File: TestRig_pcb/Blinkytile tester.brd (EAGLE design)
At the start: 160 x 140 mm, 142 parts, among them IC1 LM317BD2T, IC10 LM317BD2T, IC11 LM317BD2T, IC12 LM317BD2T, IC13 LM317BD2T, IC14 LM317BD2T, IC15 LM317BD2T, IC16 LM317BD2T, IC2 LM317BD2T, IC3 LM317BD2T, IC4 LM317BD2T, IC5 LM317BD2T, IC6 LM317BD2T, IC7 LM317BD2T, IC8 LM317BD2T, IC9 LM317BD2T, X1 MINI-USB_4P-85-32004-10X

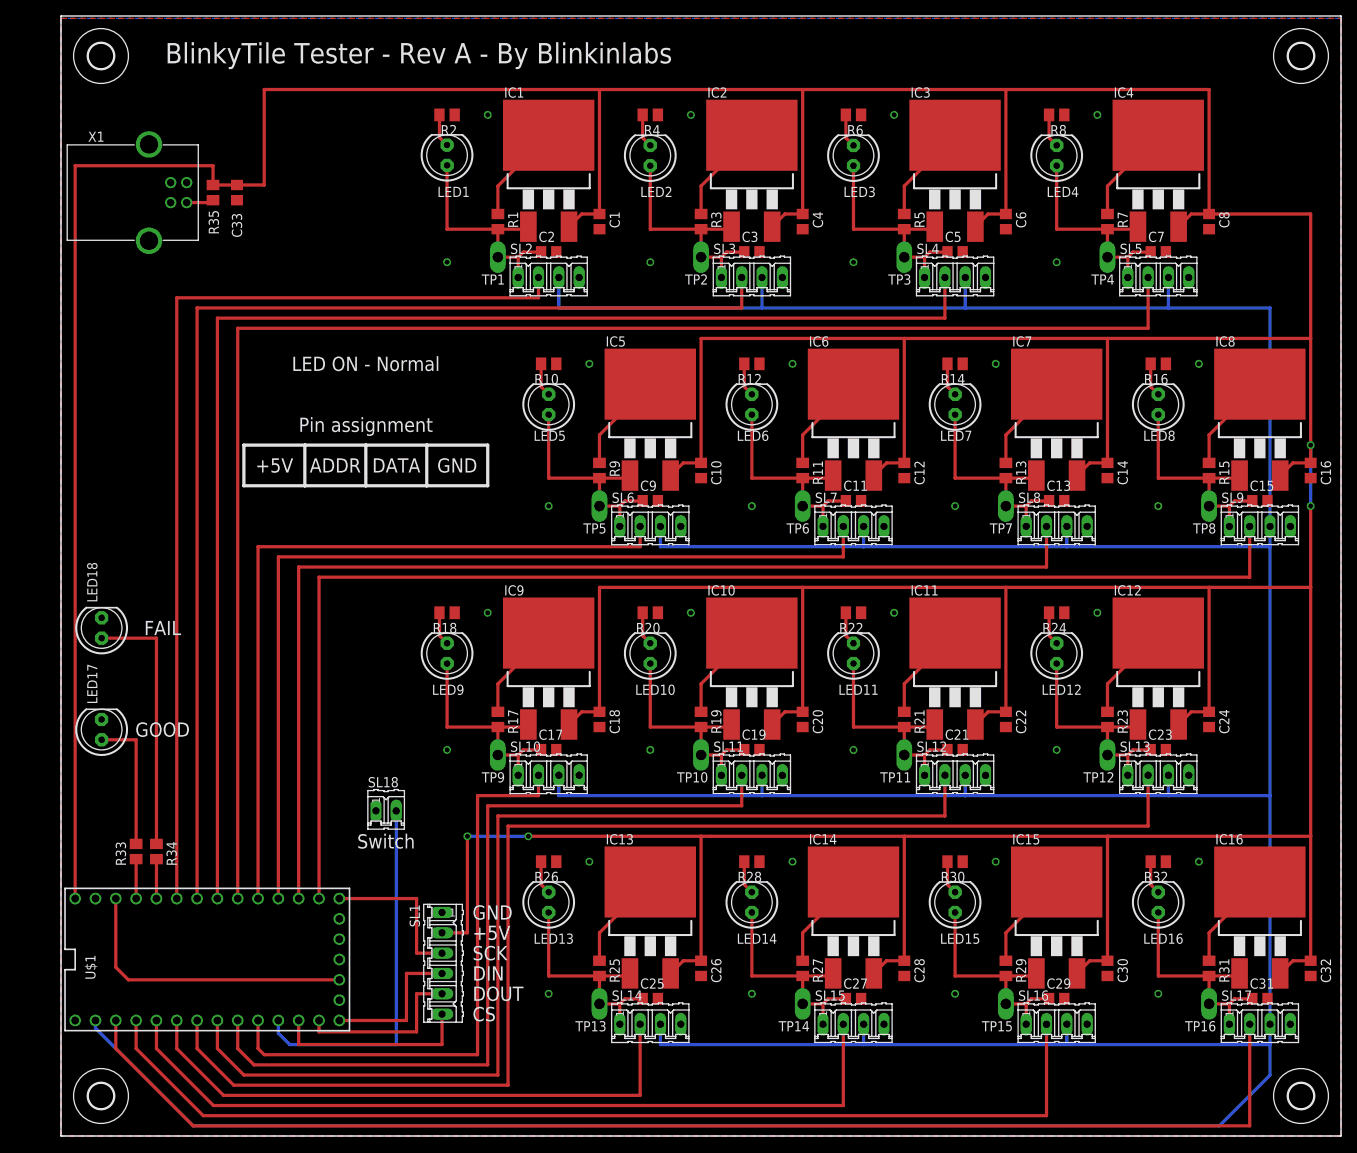
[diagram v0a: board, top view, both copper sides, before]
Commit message: RevB of tester board: add 5v buffers
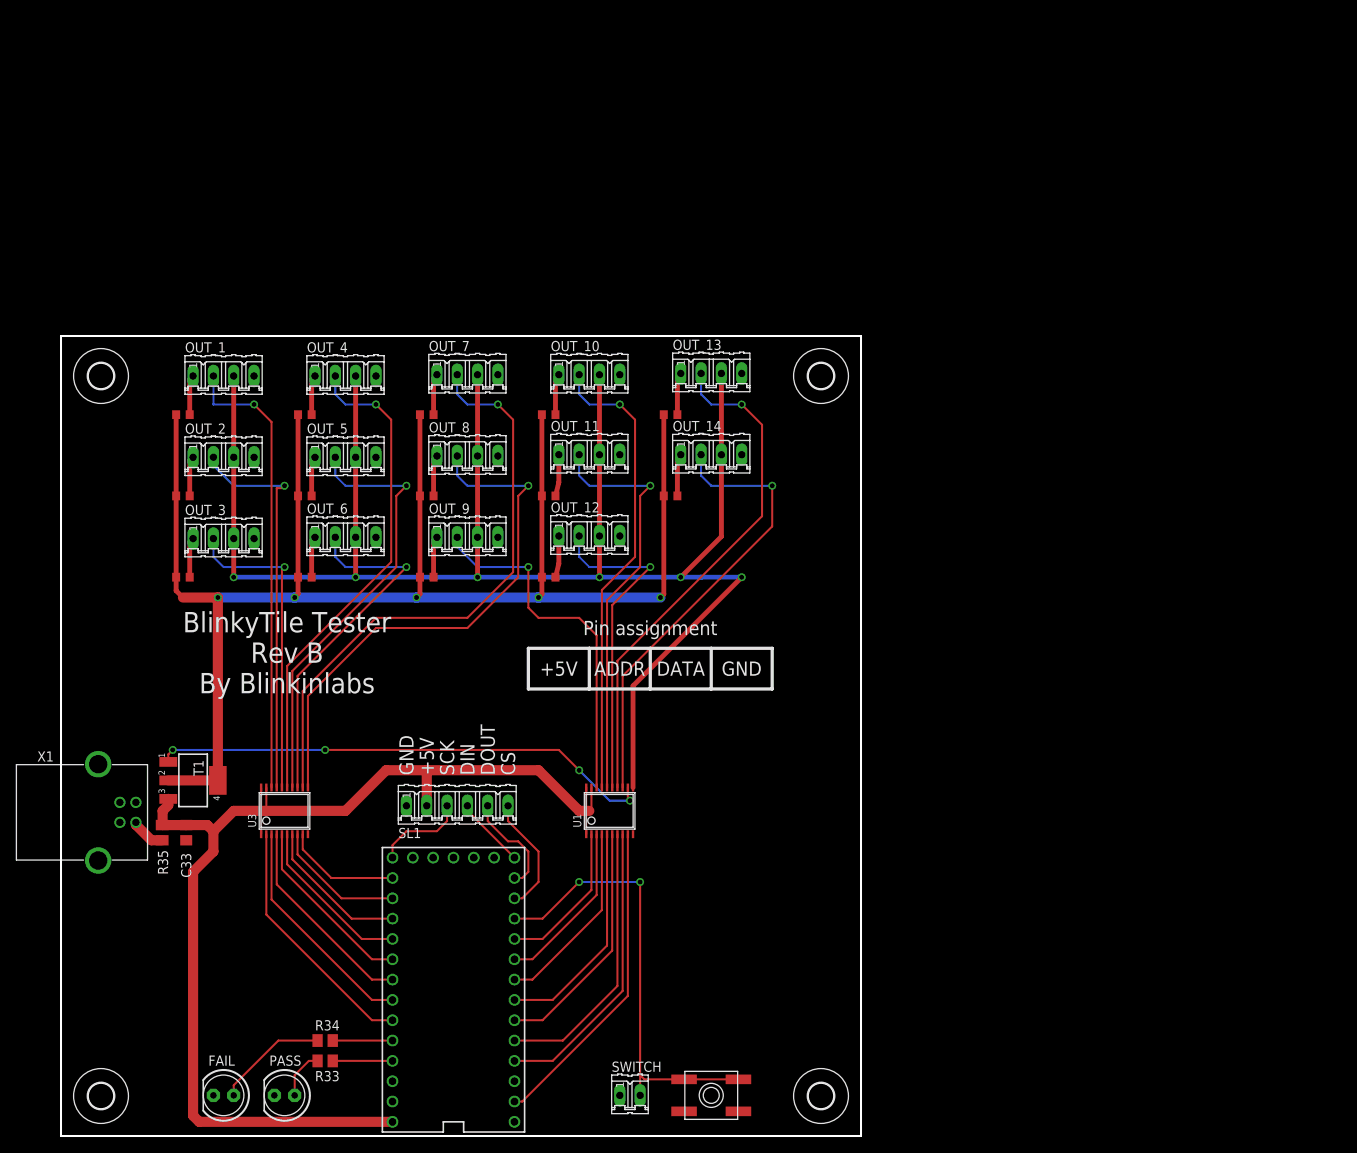
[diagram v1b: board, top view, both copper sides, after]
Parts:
- removed C1, C10, C11, C12, C13, C14, C15, C16, C17, C18, C19, C2, C20, C21, C22, C23, C24, C25, C26, C27, C28, C29, C3, C30, C31, C32, C4, C5, C6, C7, C8, C9: 0.1uF, rcl:C0805
- removed IC1, IC10, IC11, IC12, IC13, IC14, IC15, IC16, IC2, IC3, IC4, IC5, IC6, IC7, IC8, IC9: LM317BD2T, v-reg:D2PACK
- removed LED1, LED10, LED11, LED12, LED13, LED14, LED15, LED16, LED2, LED3, LED4, LED5, LED6, LED7, LED8, LED9: RED, adafruit:LED5MM
- removed LED17, LED18: (no value), adafruit:LED5MM
- removed R15, R16, R17, R18, R19, R20, R21, R22, R23, R24, R25, R26, R27, R28, R29, R30, R31, R32: (no value), rcl:M0805
- removed SL10, SL11, SL12, SL13, SL14, SL15, SL16, SL17, SL2, SL3, SL4, SL5, SL6, SL7, SL8, SL9: (no value), con-amp-quick:04P
- removed SL18: (no value), con-amp-quick:02P
- removed TP1, TP10, TP11, TP12, TP13, TP14, TP15, TP16, TP2, TP3, TP4, TP5, TP6, TP7, TP8, TP9: TPPAD1-13Y, testpad:P1-13Y
- added FAIL, PASS: (no value), adafruit:LED5MM
- added OUT_1, OUT_10, OUT_11, OUT_12, OUT_13, OUT_14, OUT_2, OUT_3, OUT_4, OUT_5, OUT_6, OUT_7, OUT_8, OUT_9: (no value), con-amp-quick:04P
- added SW1: SPST_TACT-EVQQ2, adafruit:EVQ-Q2
- added SWITCH: (no value), con-amp-quick:02P
- added T1: (no value), zetex:SOT223
- added U1, U3: SN74HCT245PWR, scanlime:TSSOP20
- R1, R10, R11, R12, R13, R14, R2, R3, R4, R5, R6, R7, R8, R9: value (none) -> 50; device rcl:M0805 -> adafruit:R0603
- moved R8 92.0 mm to (45.7, 80.0), turned to 0 degrees
- moved R6 89.7 mm to (30.5, 69.8), turned to 0 degrees
- moved R7 88.4 mm to (45.7, 90.2), turned to 0 degrees
- moved R5 82.4 mm to (30.5, 80.0), turned to 0 degrees
- moved C33 80.3 mm to (15.7, 37.9)
- moved R35 80.3 mm to (12.7, 37.9)
- moved R3 78.6 mm to (15.2, 69.8), turned to 0 degrees
- moved X1 77.7 mm to (4.65, 40.5)
- moved H3 72.1 mm to (95.0, 95.0)
- moved H4 60.0 mm to (95.0, 5.00)
- moved R2 58.0 mm to (15.2, 80.0), turned to 0 degrees
- moved R4 57.2 mm to (30.5, 90.2), turned to 0 degrees
- moved R1 46.2 mm to (15.2, 90.2), turned to 0 degrees
- moved R13 42.5 mm to (76.2, 90.2), turned to 0 degrees
- moved H2 40.0 mm to (5.00, 95.0)
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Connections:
- removed net ADDR15: SL16.2, U$1.2
- removed net ADDR16: SL17.2, U$1.1
- removed net N$10: IC4.2, R7.1
- removed net N$12: LED4.K, R8.2
- removed net N$13: IC5.2, R9.1
- removed net N$14: C9.1, IC5.1, LED5.A, R9.2, SL6.1, TP5.TP
- removed net N$15: LED5.K, R10.2
- removed net N$16: IC6.2, R11.1
- removed net N$18: LED6.K, R12.2
- removed net N$19: IC7.2, R13.1
- removed net N$21: LED7.K, R14.2
- removed net N$22: IC8.2, R15.1
- removed net N$24: LED8.K, R16.2
- removed net N$25: IC9.2, R17.1
- removed net N$27: LED9.K, R18.2
- removed net N$28: IC10.2, R19.1
- removed net N$30: LED10.K, R20.2
- removed net N$31: IC11.2, R21.1
- removed net N$33: LED11.K, R22.2
- removed net N$34: IC12.2, R23.1
- removed net N$35: C23.1, IC12.1, LED12.A, R23.2, SL13.1, TP12.TP
- removed net N$36: LED12.K, R24.2
- removed net N$37: IC13.2, R25.1
- removed net N$39: LED13.K, R26.2
- removed net N$40: IC14.2, R27.1
- removed net N$42: LED14.K, R28.2
- removed net N$43: IC15.2, R29.1
- removed net N$45: LED15.K, R30.2
- removed net N$46: IC16.2, R31.1
- removed net N$47: C31.1, IC16.1, LED16.A, R31.2, SL17.1, TP16.TP
- removed net N$48: LED16.K, R32.2
- removed net N$5: LED1.K, R2.2
- removed net N$51: LED17.A, R33.1
- removed net N$54: SL18.2, U$1.9
- removed net N$6: LED2.K, R4.2
- removed net N$7: IC3.2, R5.1
- removed net N$9: LED3.K, R6.2
- new net 5V_B: R1.1, R10.1, R11.1, R12.1, R13.1, R14.1, R2.1, R3.1, R4.1, R5.1, R6.1, R7.1, R8.1, R9.1, T1.2, T1.4
- new net ADDR10_B: OUT_10.2, U1.17
- new net ADDR11_B: OUT_11.2, U1.16
- new net ADDR12_B: OUT_12.2, U1.15
- new net ADDR13_B: OUT_13.2, U1.14
- new net ADDR14_B: OUT_14.2, U1.13
- new net ADDR1_B: OUT_1.2, U3.18
- new net ADDR2_B: OUT_2.2, U3.17
- new net ADDR3_B: OUT_3.2, U3.16
- new net ADDR4_B: OUT_4.2, U3.15
- new net ADDR5_B: OUT_5.2, U3.14
- new net ADDR6_B: OUT_6.2, U3.13
- new net ADDR7_B: OUT_7.2, U3.12
- new net ADDR8_B: OUT_8.2, U3.11
- new net ADDR9_B: OUT_9.2, U1.18
- new net DATA_B: OUT_1.3, OUT_10.3, OUT_11.3, OUT_12.3, OUT_13.3, OUT_14.3, OUT_2.3, OUT_3.3, OUT_4.3, OUT_5.3, OUT_6.3, OUT_7.3, OUT_8.3, OUT_9.3, U1.11
- new net GOOD: PASS.A, R33.1
- new net PWR_EN: U$1.2, U1.8
- new net PWR_EN_B: T1.1, U1.12
- net +5V: now also T1.3, U1.1, U1.19, U1.20, U3.1, U3.19, U3.20; no longer C1.1, C10.1, C12.1, C14.1, C16.1, C18.1, C20.1, C22.1, C24.1, C26.1, C28.1, C30.1, C32.1, C4.1, C6.1, C8.1, IC1.3, IC10.3, IC11.3, IC12.3, IC13.3, IC14.3, IC15.3, IC16.3, IC2.3, IC3.3, IC4.3, IC5.3, IC6.3, IC7.3, IC8.3, IC9.3
- net ADDR1: now also U3.2; no longer SL2.2
- net ADDR10: now also U1.3; no longer SL11.2
- net ADDR11: now also U1.4; no longer SL12.2
- net ADDR12: now also U1.5; no longer SL13.2
- net ADDR13: now also U1.6; no longer SL14.2
- net ADDR14: now also U1.7; no longer SL15.2
- net ADDR2: now also U3.3; no longer SL3.2
- net ADDR3: now also U3.4; no longer SL4.2
- net ADDR4: now also U3.5; no longer SL5.2
- net ADDR5: now also U3.6; no longer SL6.2
- net ADDR6: now also U3.7; no longer SL7.2
- net ADDR7: now also U3.8; no longer SL8.2
- net ADDR8: now also U3.9; no longer SL9.2
- net ADDR9: now also U1.2; no longer SL10.2
- net DATA: now also U1.9; no longer SL10.3, SL11.3, SL12.3, SL13.3, SL14.3, SL15.3, SL16.3, SL17.3, SL2.3, SL3.3, SL4.3, SL5.3, SL6.3, SL7.3, SL8.3, SL9.3
- net GND: now also FAIL.K, OUT_1.4, OUT_10.4, OUT_11.4, OUT_12.4, OUT_13.4, OUT_14.4, OUT_2.4, OUT_3.4, OUT_4.4, OUT_5.4, OUT_6.4, OUT_7.4, OUT_8.4, OUT_9.4, PASS.K, SW1.A, SW1.A', SWITCH.1, U1.10, U3.10; no longer C1.2, C10.2, C11.2, C12.2, C13.2, C14.2, C15.2, C16.2, C17.2, C18.2, C19.2, C2.2, C20.2, C21.2, C22.2, C23.2, C24.2, C25.2, C26.2, C27.2, C28.2, C29.2, C3.2, C30.2, C31.2, C32.2, C4.2, C5.2, C6.2, C7.2, C8.2, C9.2, LED17.K, LED18.K, R10.1, R12.1, R14.1, R16.1, R18.1, R2.1, R20.1, R22.1, R24.1, R26.1, R28.1, R30.1, R32.1, R4.1, R6.1, R8.1, SL10.4, SL11.4, SL12.4, SL13.4, SL14.4, SL15.4, SL16.4, SL17.4, SL18.1, SL2.4, SL3.4, SL4.4, SL5.4, SL6.4, SL7.4, SL8.4, SL9.4
- net N$1: now also OUT_5.1, R5.2; no longer IC1.2, R1.1
- net N$11: now also OUT_4.1, R4.2; no longer C7.1, IC4.1, LED4.A, R7.2, SL5.1, TP4.TP
- net N$17: now also OUT_6.1, R6.2; no longer C11.1, IC6.1, LED6.A, R11.2, SL7.1, TP6.TP
- net N$2: now also OUT_1.1; no longer C2.1, IC1.1, LED1.A, SL2.1, TP1.TP
- net N$20: now also OUT_7.1, R7.2; no longer C13.1, IC7.1, LED7.A, R13.2, SL8.1, TP7.TP
- net N$23: now also OUT_8.1, R8.2; no longer C15.1, IC8.1, LED8.A, R15.2, SL9.1, TP8.TP
- net N$26: now also OUT_9.1, R9.2; no longer C17.1, IC9.1, LED9.A, R17.2, SL10.1, TP9.TP
- net N$29: now also OUT_10.1, R10.2; no longer C19.1, IC10.1, LED10.A, R19.2, SL11.1, TP10.TP
- net N$3: now also SW1.B, SW1.B', SWITCH.2, U$1.9; no longer IC2.2, R3.1
- net N$32: now also OUT_11.1, R11.2; no longer C21.1, IC11.1, LED11.A, R21.2, SL12.1, TP11.TP
- net N$38: now also OUT_13.1, R13.2; no longer C25.1, IC13.1, LED13.A, R25.2, SL14.1, TP13.TP
- net N$4: now also OUT_2.1, R2.2; no longer C3.1, IC2.1, LED2.A, R3.2, SL3.1, TP2.TP
- net N$41: now also OUT_14.1, R14.2; no longer C27.1, IC14.1, LED14.A, R27.2, SL15.1, TP14.TP
- net N$44: now also OUT_12.1, R12.2; no longer C29.1, IC15.1, LED15.A, R29.2, SL16.1, TP15.TP
- net N$52: now also FAIL.A; no longer LED18.A
- net N$8: now also OUT_3.1, R3.2; no longer C5.1, IC3.1, LED3.A, R5.2, SL4.1, TP3.TP
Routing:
- net +5V: track 931.0 -> 147.2 mm, vias 4 -> 0
- net DATA: track 622.2 -> 39.9 mm
- net DATA_B: track 0.00 -> 223.9 mm, vias 0 -> 6
- net 5V_B: track 0.00 -> 204.1 mm, vias 0 -> 5
- net ADDR4: track 191.4 -> 22.9 mm
- net ADDR16: track 162.0 -> 0.00 mm
- net ADDR8: track 162.9 -> 14.6 mm
- net ADDR3: track 168.6 -> 25.7 mm
- net ADDR12: track 163.0 -> 28.3 mm
- net ADDR15: track 132.2 -> 0.00 mm
- net ADDR7: track 140.0 -> 16.7 mm
- net ADDR2: track 145.7 -> 28.5 mm
- net ADDR11: track 133.3 -> 24.0 mm
- net ADDR6: track 117.1 -> 18.7 mm
- net ADDR1: track 122.9 -> 31.3 mm
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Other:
- board size 160 x 140 mm -> 100 x 100 mm
- board text added: "BlinkyTile Tester Rev B By Blinkinlabs"
- board text removed: "BlinkyTile Tester - Rev A - By Blinkinlabs"
- board text removed: "FAIL"
- board text removed: "GOOD"
- board text removed: "LED ON - Normal"
- board text removed: "Switch"
